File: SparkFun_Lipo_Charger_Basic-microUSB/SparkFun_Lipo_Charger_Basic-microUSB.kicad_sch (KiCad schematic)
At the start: 16 parts, among them U1 MCP73831

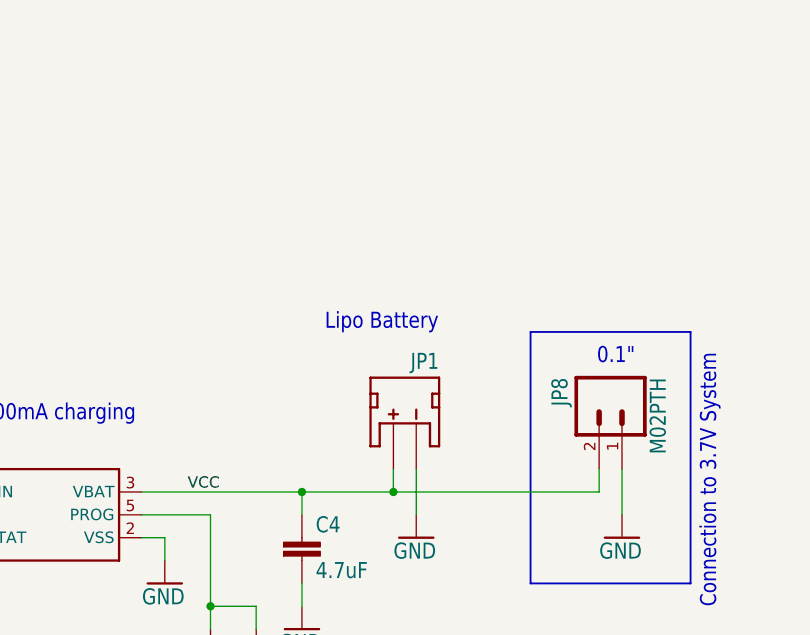
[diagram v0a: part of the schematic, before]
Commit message: add lipo charger
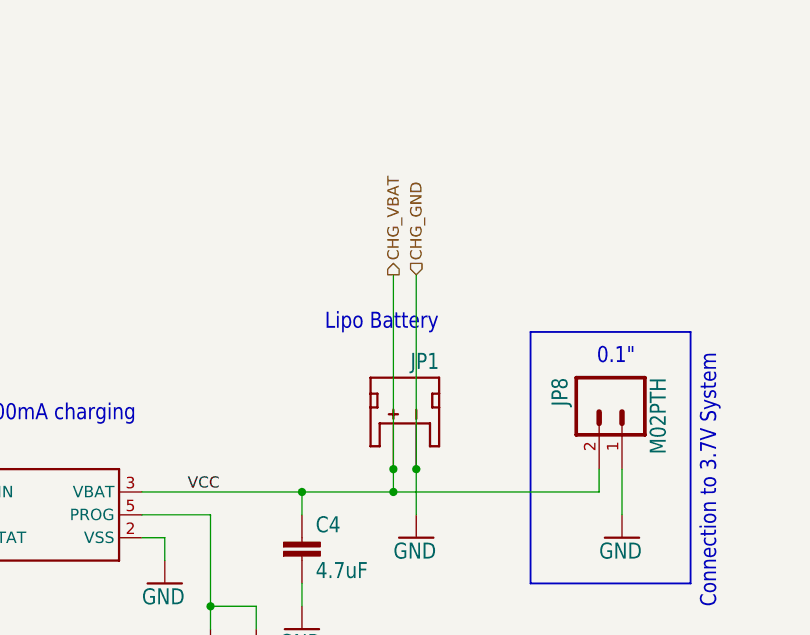
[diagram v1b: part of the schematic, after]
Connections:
- net VCC renamed CHG_VBAT
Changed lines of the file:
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@@
   (junction (at 165.1 83.82) (diameter 0) (color 0 0 0 0)
+  )
+  (junction (at 177.8 81.28) (diameter 0) (color 0 0 0 0)
+  )
+  (junction (at 175.26 81.28) (diameter 0) (color 0 0 0 0)
   )
   (junction (at 109.22 83.82) (diameter 0) (color 0 0 0 0)
@@
     (stroke (width 0.1524) (type solid))
   )
+  (wire (pts (xy 175.26 59.69) (xy 175.26 81.28))
+    (stroke (width 0) (type default))
+  )
   (wire (pts (xy 154.94 114.3) (xy 154.94 111.76))
     (stroke (width 0.1524) (type solid))
@@
     (stroke (width 0.1524) (type solid))
   )
+  (wire (pts (xy 177.8 59.69) (xy 177.8 81.28))
+    (stroke (width 0) (type default))
+  )
   (wire (pts (xy 200.66 81.28) (xy 200.66 86.36))
     (stroke (width 0.1524) (type solid))
@@
   (label "VIN" (at 111.76 83.82 0) (fields_autoplaced)
     (effects (font (size 1.2446 1.2446)) (justify left bottom))
+  )
+  (hierarchical_label "CHG_GND" (shape input) (at 177.8 59.69 90) (fields_autoplaced)
+    (effects (font (size 1.27 1.27)) (justify left))
+  )
+  (hierarchical_label "CHG_VBAT" (shape output) (at 175.26 59.69 90) (fields_autoplaced)
+    (effects (font (size 1.27 1.27)) (justify left))
   )
   (symbol (lib_id "SparkFun_Lipo_Charger_Basic-microUSB-eagle-import:USB-ABCONN-11794") (at 86.36 88.9 180) (unit 1)
@@
         )
       )
+      (project "aps490_detection"
+        (path "/e118c919-9296-4265-a7f4-7c13f94290b1/bad03448-3ebc-42d0-be48-dd19294cc20c/0189be23-f30a-49a0-a245-8d28dabd251c"
+          (reference "JP9") (unit 1)
+        )
+      )
     )
   )
@@
         )
       )
+      (project "aps490_detection"
+        (path "/e118c919-9296-4265-a7f4-7c13f94290b1/bad03448-3ebc-42d0-be48-dd19294cc20c/0189be23-f30a-49a0-a245-8d28dabd251c"
+          (reference "JP2") (unit 1)
+        )
+      )
     )
   )
@@
         )
       )
+      (project "aps490_detection"
+        (path "/e118c919-9296-4265-a7f4-7c13f94290b1/bad03448-3ebc-42d0-be48-dd19294cc20c/0189be23-f30a-49a0-a245-8d28dabd251c"
+          (reference "R4") (unit 1)
+        )
+      )
     )
   )
@@
         )
       )
+      (project "aps490_detection"
+        (path "/e118c919-9296-4265-a7f4-7c13f94290b1/bad03448-3ebc-42d0-be48-dd19294cc20c/0189be23-f30a-49a0-a245-8d28dabd251c"
+          (reference "#GND17") (unit 1)
+        )
+      )
     )
   )
@@
       (project "SparkFun_Lipo_Charger_Basic-microUSB"
         (path "/342e9741-5281-407b-be73-39ccad418930"
+          (reference "R3") (unit 1)
+        )
+      )
+      (project "aps490_detection"
+        (path "/e118c919-9296-4265-a7f4-7c13f94290b1/bad03448-3ebc-42d0-be48-dd19294cc20c/0189be23-f30a-49a0-a245-8d28dabd251c"
           (reference "R3") (unit 1)
         )
@@
         )
       )
+      (project "aps490_detection"
+        (path "/e118c919-9296-4265-a7f4-7c13f94290b1/bad03448-3ebc-42d0-be48-dd19294cc20c/0189be23-f30a-49a0-a245-8d28dabd251c"
+          (reference "U1") (unit 1)
+        )
+      )
     )
   )
@@
         )
       )
+      (project "aps490_detection"
+        (path "/e118c919-9296-4265-a7f4-7c13f94290b1/bad03448-3ebc-42d0-be48-dd19294cc20c/0189be23-f30a-49a0-a245-8d28dabd251c"
+          (reference "D11") (unit 1)
+        )
+      )
     )
   )
@@
         )
       )
+      (project "aps490_detection"
+        (path "/e118c919-9296-4265-a7f4-7c13f94290b1/bad03448-3ebc-42d0-be48-dd19294cc20c/0189be23-f30a-49a0-a245-8d28dabd251c"
+          (reference "#GND1") (unit 1)
+        )
+      )
     )
   )
@@
         )
       )
+      (project "aps490_detection"
+        (path "/e118c919-9296-4265-a7f4-7c13f94290b1/bad03448-3ebc-42d0-be48-dd19294cc20c/0189be23-f30a-49a0-a245-8d28dabd251c"
+          (reference "C3") (unit 1)
+        )
+      )
     )
   )
@@
         )
       )
+      (project "aps490_detection"
+        (path "/e118c919-9296-4265-a7f4-7c13f94290b1/bad03448-3ebc-42d0-be48-dd19294cc20c/0189be23-f30a-49a0-a245-8d28dabd251c"
+          (reference "LOGO1") (unit 1)
+        )
+      )
     )
   )
@@
         )
       )
+      (project "aps490_detection"
+        (path "/e118c919-9296-4265-a7f4-7c13f94290b1/bad03448-3ebc-42d0-be48-dd19294cc20c/0189be23-f30a-49a0-a245-8d28dabd251c"
+          (reference "#GND2") (unit 1)
+        )
+      )
     )
   )
@@
         )
       )
+      (project "aps490_detection"
+        (path "/e118c919-9296-4265-a7f4-7c13f94290b1/bad03448-3ebc-42d0-be48-dd19294cc20c/0189be23-f30a-49a0-a245-8d28dabd251c"
+          (reference "JP8") (unit 1)
+        )
+      )
     )
   )
@@
         )
       )
+      (project "aps490_detection"
+        (path "/e118c919-9296-4265-a7f4-7c13f94290b1/bad03448-3ebc-42d0-be48-dd19294cc20c/0189be23-f30a-49a0-a245-8d28dabd251c"
+          (reference "FRAME1") (unit 2)
+        )
+      )
     )
   )
@@
         )
       )
+      (project "aps490_detection"
+        (path "/e118c919-9296-4265-a7f4-7c13f94290b1/bad03448-3ebc-42d0-be48-dd19294cc20c/0189be23-f30a-49a0-a245-8d28dabd251c"
+          (reference "#GND18") (unit 1)
+        )
+      )
     )
   )
@@
         )
       )
+      (project "aps490_detection"
+        (path "/e118c919-9296-4265-a7f4-7c13f94290b1/bad03448-3ebc-42d0-be48-dd19294cc20c/0189be23-f30a-49a0-a245-8d28dabd251c"
+          (reference "#GND14") (unit 1)
+        )
+      )
     )
   )
@@
         )
       )
+      (project "aps490_detection"
+        (path "/e118c919-9296-4265-a7f4-7c13f94290b1/bad03448-3ebc-42d0-be48-dd19294cc20c/0189be23-f30a-49a0-a245-8d28dabd251c"
+          (reference "#GND19") (unit 1)
+        )
+      )
     )
   )
@@
         )
       )
+      (project "aps490_detection"
+        (path "/e118c919-9296-4265-a7f4-7c13f94290b1/bad03448-3ebc-42d0-be48-dd19294cc20c/0189be23-f30a-49a0-a245-8d28dabd251c"
+          (reference "C4") (unit 1)
+        )
+      )
     )
   )
@@
         )
       )
+      (project "aps490_detection"
+        (path "/e118c919-9296-4265-a7f4-7c13f94290b1/bad03448-3ebc-42d0-be48-dd19294cc20c/0189be23-f30a-49a0-a245-8d28dabd251c"
+          (reference "JP4") (unit 1)
+        )
+      )
     )
   )
@@
         )
       )
+      (project "aps490_detection"
+        (path "/e118c919-9296-4265-a7f4-7c13f94290b1/bad03448-3ebc-42d0-be48-dd19294cc20c/0189be23-f30a-49a0-a245-8d28dabd251c"
+          (reference "LOGO2") (unit 1)
+        )
+      )
     )
   )
@@
         )
       )
+      (project "aps490_detection"
+        (path "/e118c919-9296-4265-a7f4-7c13f94290b1/bad03448-3ebc-42d0-be48-dd19294cc20c/0189be23-f30a-49a0-a245-8d28dabd251c"
+          (reference "#GND15") (unit 1)
+        )
+      )
     )
   )
@@
       (project "SparkFun_Lipo_Charger_Basic-microUSB"
         (path "/342e9741-5281-407b-be73-39ccad418930"
+          (reference "FRAME1") (unit 1)
+        )
+      )
+      (project "aps490_detection"
+        (path "/e118c919-9296-4265-a7f4-7c13f94290b1/bad03448-3ebc-42d0-be48-dd19294cc20c/0189be23-f30a-49a0-a245-8d28dabd251c"
           (reference "FRAME1") (unit 1)
         )
@@
         )
       )
+      (project "aps490_detection"
+        (path "/e118c919-9296-4265-a7f4-7c13f94290b1/bad03448-3ebc-42d0-be48-dd19294cc20c/0189be23-f30a-49a0-a245-8d28dabd251c"
+          (reference "JP1") (unit 1)
+        )
+      )
     )
   )
@@
       (project "SparkFun_Lipo_Charger_Basic-microUSB"
         (path "/342e9741-5281-407b-be73-39ccad418930"
+          (reference "JP3") (unit 1)
+        )
+      )
+      (project "aps490_detection"
+        (path "/e118c919-9296-4265-a7f4-7c13f94290b1/bad03448-3ebc-42d0-be48-dd19294cc20c/0189be23-f30a-49a0-a245-8d28dabd251c"
           (reference "JP3") (unit 1)
         )
@@
         )
       )
-    )
-  )
-  (sheet_instances
-    (path "/" (page "1"))
+      (project "aps490_detection"
+        (path "/e118c919-9296-4265-a7f4-7c13f94290b1/bad03448-3ebc-42d0-be48-dd19294cc20c/0189be23-f30a-49a0-a245-8d28dabd251c"
+          (reference "R1") (unit 1)
+        )
+      )
+    )
   )
 )
